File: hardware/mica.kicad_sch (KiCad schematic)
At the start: 29 parts, among them J1 USB_C_Receptacle_USB2.0, J2 Conn_ARM_JTAG_SWD_10, SW1 SW_Push, U1 STM32F072C8Tx, U2 MIC5205-3.3YM5

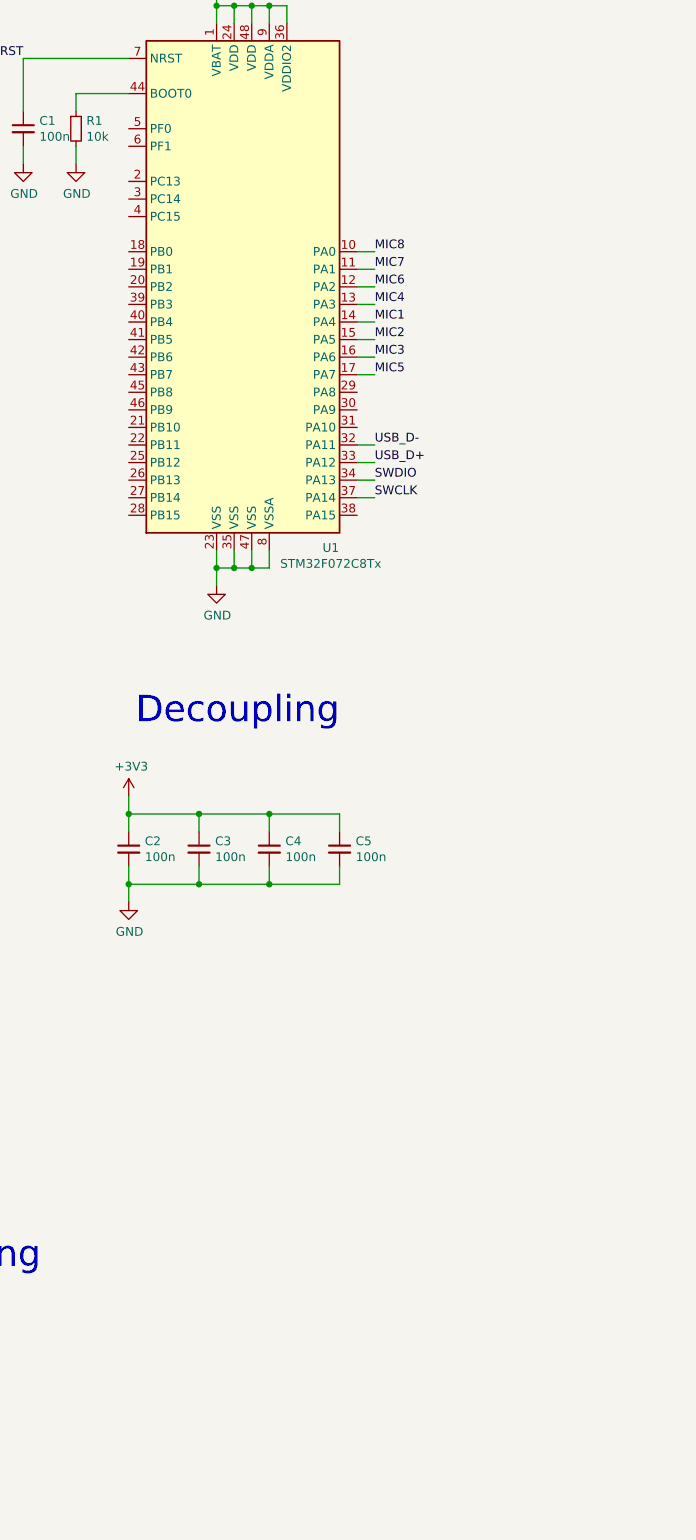
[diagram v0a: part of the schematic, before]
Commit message: Fix all ERC errors
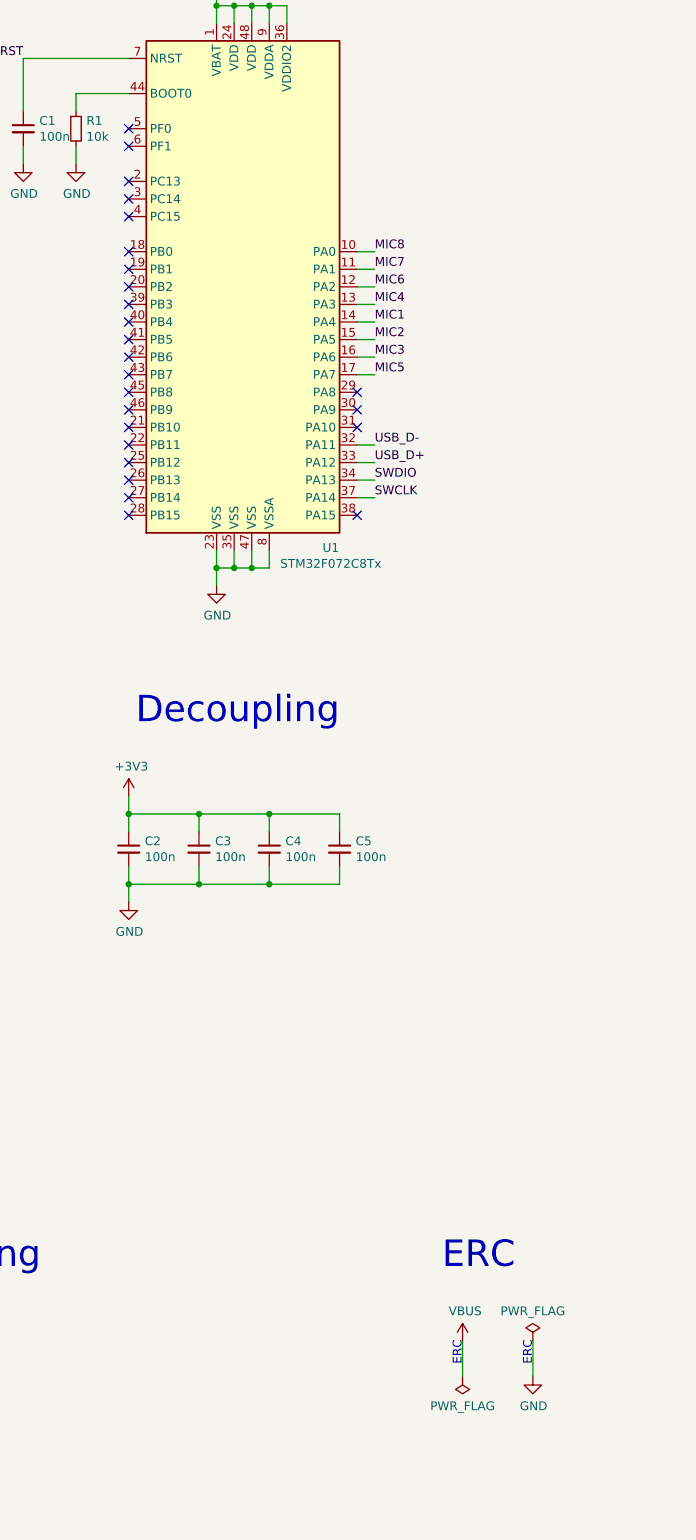
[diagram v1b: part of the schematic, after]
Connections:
- no-connect marks 4 -> 29
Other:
- note added: "ERC"
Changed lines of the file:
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@@
   (junction (at 160.02 86.36) (diameter 0.9144) (color 0 0 0 0))
   (junction (at 218.44 119.38) (diameter 0.9144) (color 0 0 0 0))
+  (no_connect (at 58.42 185.42))
+  (no_connect (at 58.42 187.96))
+  (no_connect (at 58.42 193.04))
+  (no_connect (at 58.42 195.58))
+  (no_connect (at 58.42 198.12))
+  (no_connect (at 58.42 203.2))
+  (no_connect (at 58.42 205.74))
+  (no_connect (at 58.42 208.28))
+  (no_connect (at 58.42 210.82))
+  (no_connect (at 58.42 213.36))
+  (no_connect (at 58.42 215.9))
+  (no_connect (at 58.42 218.44))
+  (no_connect (at 58.42 220.98))
+  (no_connect (at 58.42 223.52))
+  (no_connect (at 58.42 226.06))
+  (no_connect (at 58.42 228.6))
+  (no_connect (at 58.42 231.14))
+  (no_connect (at 58.42 233.68))
+  (no_connect (at 58.42 236.22))
+  (no_connect (at 58.42 238.76))
+  (no_connect (at 58.42 241.3))
   (no_connect (at 76.2 114.3))
   (no_connect (at 76.2 116.84))
+  (no_connect (at 91.44 223.52))
+  (no_connect (at 91.44 226.06))
+  (no_connect (at 91.44 228.6))
+  (no_connect (at 91.44 241.3))
   (no_connect (at 231.14 104.14))
   (no_connect (at 231.14 106.68))
@@
     (stroke (width 0) (type solid) (color 0 0 0 0))
   )
+  (wire (pts (xy 106.68 360.68) (xy 106.68 365.76))
+    (stroke (width 0) (type solid) (color 0 0 0 0))
+  )
+  (wire (pts (xy 116.84 360.68) (xy 116.84 365.76))
+    (stroke (width 0) (type solid) (color 0 0 0 0))
+  )
   (wire (pts (xy 127 83.82) (xy 127 86.36))
     (stroke (width 0) (type solid) (color 0 0 0 0))
@@
     (effects (font (size 3.81 3.81)) (justify right bottom))
   )
+  (text "ERC" (at 106.68 360.68 270)
+    (effects (font (size 1.27 1.27)) (justify right bottom))
+  )
+  (text "ERC" (at 114.3 350.52 180)
+    (effects (font (size 3.81 3.81)) (justify right bottom))
+  )
+  (text "ERC" (at 116.84 360.68 270)
+    (effects (font (size 1.27 1.27)) (justify right bottom))
+  )
   (text "3.3V regulator" (at 165.1 73.66 180)
     (effects (font (size 3.81 3.81)) (justify right bottom))
@@
     (effects (font (size 1.27 1.27)) (justify left bottom))
   )
+  (symbol (lib_id "power:PWR_FLAG") (at 106.68 365.76 180) (unit 1)
+    (in_bom yes) (on_board yes)
+    (property "Reference" "#FLG0101" (id 0) (at 106.68 367.665 0)
+      (effects (font (size 1.27 1.27)) hide)
+    )
+    (property "Value" "PWR_FLAG" (id 1) (at 106.68 370.0844 0))
+    (property "Footprint" "" (id 2) (at 106.68 365.76 0)
+      (effects (font (size 1.27 1.27)) hide)
+    )
+    (property "Datasheet" "~" (id 3) (at 106.68 365.76 0)
+      (effects (font (size 1.27 1.27)) hide)
+    )
+    (pin "1")
+  )
+  (symbol (lib_id "power:PWR_FLAG") (at 116.84 360.68 0) (unit 1)
+    (in_bom yes) (on_board yes)
+    (property "Reference" "#FLG?" (id 0) (at 116.84 358.775 0)
+      (effects (font (size 1.27 1.27)) hide)
+    )
+    (property "Value" "PWR_FLAG" (id 1) (at 116.84 356.3556 0))
+    (property "Footprint" "" (id 2) (at 116.84 360.68 0)
+      (effects (font (size 1.27 1.27)) hide)
+    )
+    (property "Datasheet" "~" (id 3) (at 116.84 360.68 0)
+      (effects (font (size 1.27 1.27)) hide)
+    )
+    (pin "1")
+  )
   (symbol (lib_id "power:+3V3") (at 58.42 281.94 0) (unit 1)
     (in_bom yes) (on_board yes)
@@
     (pin "1")
   )
+  (symbol (lib_id "power:VBUS") (at 106.68 360.68 0) (unit 1)
+    (in_bom yes) (on_board yes)
+    (property "Reference" "#PWR0140" (id 0) (at 106.68 364.49 0)
+      (effects (font (size 1.27 1.27)) hide)
+    )
+    (property "Value" "VBUS" (id 1) (at 107.0483 356.3556 0))
+    (property "Footprint" "" (id 2) (at 106.68 360.68 0)
+      (effects (font (size 1.27 1.27)) hide)
+    )
+    (property "Datasheet" "" (id 3) (at 106.68 360.68 0)
+      (effects (font (size 1.27 1.27)) hide)
+    )
+    (pin "1")
+  )
   (symbol (lib_id "power:VBUS") (at 127 83.82 0) (unit 1)
     (in_bom yes) (on_board yes)
@@
     )
     (property "Datasheet" "" (id 3) (at 99.06 104.14 0)
+      (effects (font (size 1.27 1.27)) hide)
+    )
+    (pin "1")
+  )
+  (symbol (lib_id "power:GND") (at 116.84 365.76 0) (unit 1)
+    (in_bom yes) (on_board yes)
+    (property "Reference" "#PWR?" (id 0) (at 116.84 372.11 0)
+      (effects (font (size 1.27 1.27)) hide)
+    )
+    (property "Value" "GND" (id 1) (at 116.9543 370.0844 0))
+    (property "Footprint" "" (id 2) (at 116.84 365.76 0)
+      (effects (font (size 1.27 1.27)) hide)
+    )
+    (property "Datasheet" "" (id 3) (at 116.84 365.76 0)
       (effects (font (size 1.27 1.27)) hide)
     )
@@
   )
   (symbol_instances
+    (path "/3aa08106-6228-4d8f-b8fc-92081d282ae1"
+      (reference "#FLG0101") (unit 1) (value "PWR_FLAG") (footprint "")
+    )
+    (path "/cb52e577-50e1-4bad-b009-49bdbe72b262"
+      (reference "#FLG?") (unit 1) (value "PWR_FLAG") (footprint "")
+    )
     (path "/ecbc8434-dd2d-4b30-a9cc-c58a56058b10"
       (reference "#PWR01") (unit 1) (value "GND") (footprint "")
@@
       (reference "#PWR019") (unit 1) (value "+3V3") (footprint "")
     )
+    (path "/1e0ff577-e611-44f3-8708-d88e045903c0"
+      (reference "#PWR0140") (unit 1) (value "VBUS") (footprint "")
+    )
+    (path "/2bf07272-5fec-49bc-a787-04a8c4649f10"
+      (reference "#PWR?") (unit 1) (value "GND") (footprint "")
+    )
     (path "/96a8602f-0762-4f84-9239-5b1519e271de"

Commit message: Assign footprints
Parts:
- C1, C2, C3, C4, C5: footprint (none) -> Capacitor_SMD:C_0402_1005Metric; Dielectric - -> X7R; MPN (none) -> 885012205018; Voltage 6.3V -> 10V
- C6, C8: footprint (none) -> Capacitor_SMD:C_0402_1005Metric; Dielectric - -> X7R; MPN (none) -> CL05A225MQ5NNNC; Tolerance 10% -> 20%
- C7: footprint (none) -> Capacitor_SMD:C_0402_1005Metric; Dielectric - -> X7R; MPN (none) -> 885012205059; Voltage 6.3V -> 50V
- D1: footprint (none) -> LED_SMD:LED_0603_1608Metric; MPN (none) -> 150060RS75000
- D2: footprint (none) -> LED_SMD:LED_0603_1608Metric; MPN (none) -> 150060GS75000
- F1: footprint (none) -> Fuse:Fuse_1206_3216Metric; MPN (none) -> PTS120660V005
- J1: MPN (none) -> TYPE-C-31-M-12
- J2: MPN (none) -> FTSH-105-01-L-DV-007-K

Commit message: Place button and leds pins
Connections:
- net BTN_USER: now also U1.26 (PB13)
- net LED_GREEN: now also U1.28 (PB15)
- net LED_RED: now also U1.27 (PB14)
- no-connect marks 29 -> 26

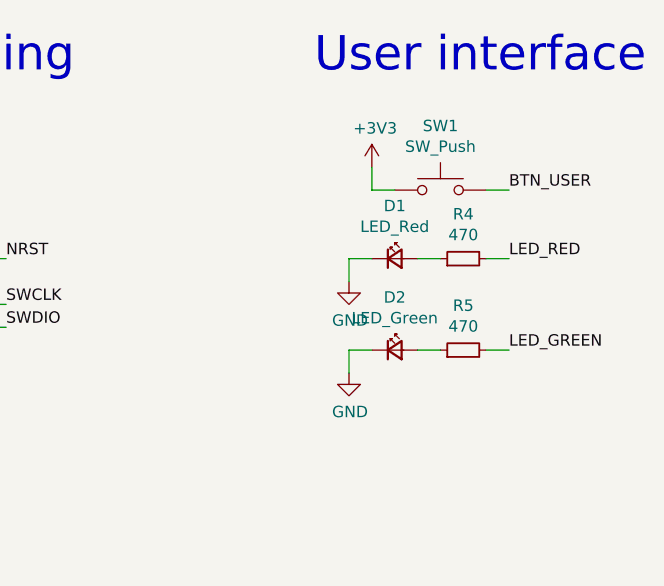
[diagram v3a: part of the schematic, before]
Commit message: Assign all footprints
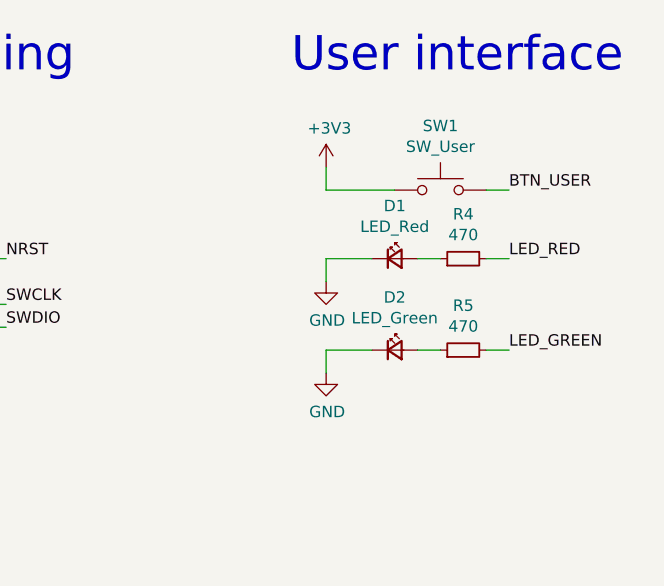
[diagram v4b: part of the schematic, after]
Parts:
- H1, H2, H3, H4, H5, H6, H7, H8: footprint (none) -> MountingHole:MountingHole_3.2mm_M3
- J2: footprint (none) -> User:Samtec_FTSH-105-01-L-DV-K; MPN FTSH-105-01-L-DV-007-K -> FTSH-105-01-L-DV-K
- R1, R2, R3, R4, R5: footprint (none) -> Resistor_SMD:R_0402_1005Metric
- SW1: value SW_Push -> SW_User; footprint (none) -> Button_Switch_THT:SW_PUSH_6mm

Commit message: Remove 4 of the 8 mounting holes
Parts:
- removed H5, H6, H7, H8: MountingHole, MountingHole:MountingHole_3.2mm_M3, symbol Mechanical:MountingHole
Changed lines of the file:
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@@
-    )
-  )
-  (symbol (lib_id "Mechanical:MountingHole") (at 22.86 381 0) (unit 1)
-    (in_bom yes) (on_board yes)
-    (property "Reference" "H5" (id 0) (at 25.4001 379.8506 0)
-      (effects (font (size 1.27 1.27)) (justify left))
-    )
-    (property "Value" "MountingHole" (id 1) (at 25.4001 382.1493 0)
-      (effects (font (size 1.27 1.27)) (justify left))
-    )
-    (property "Footprint" "MountingHole:MountingHole_3.2mm_M3" (id 2) (at 22.86 381 0)
-      (effects (font (size 1.27 1.27)) hide)
-    )
-    (property "Datasheet" "~" (id 3) (at 22.86 381 0)
-      (effects (font (size 1.27 1.27)) hide)
-    )
-  )
-  (symbol (lib_id "Mechanical:MountingHole") (at 22.86 386.08 0) (unit 1)
-    (in_bom yes) (on_board yes)
-    (property "Reference" "H6" (id 0) (at 25.4001 384.9306 0)
-      (effects (font (size 1.27 1.27)) (justify left))
-    )
-    (property "Value" "MountingHole" (id 1) (at 25.4001 387.2293 0)
-      (effects (font (size 1.27 1.27)) (justify left))
-    )
-    (property "Footprint" "MountingHole:MountingHole_3.2mm_M3" (id 2) (at 22.86 386.08 0)
-      (effects (font (size 1.27 1.27)) hide)
-    )
-    (property "Datasheet" "~" (id 3) (at 22.86 386.08 0)
-      (effects (font (size 1.27 1.27)) hide)
-    )
-  )
-  (symbol (lib_id "Mechanical:MountingHole") (at 22.86 391.16 0) (unit 1)
-    (in_bom yes) (on_board yes)
-    (property "Reference" "H7" (id 0) (at 25.4001 390.0106 0)
-      (effects (font (size 1.27 1.27)) (justify left))
-    )
-    (property "Value" "MountingHole" (id 1) (at 25.4001 392.3093 0)
-      (effects (font (size 1.27 1.27)) (justify left))
-    )
-    (property "Footprint" "MountingHole:MountingHole_3.2mm_M3" (id 2) (at 22.86 391.16 0)
-      (effects (font (size 1.27 1.27)) hide)
-    )
-    (property "Datasheet" "~" (id 3) (at 22.86 391.16 0)
-      (effects (font (size 1.27 1.27)) hide)
-    )
-  )
-  (symbol (lib_id "Mechanical:MountingHole") (at 22.86 396.24 0) (unit 1)
-    (in_bom yes) (on_board yes)
-    (property "Reference" "H8" (id 0) (at 25.4001 395.0906 0)
-      (effects (font (size 1.27 1.27)) (justify left))
-    )
-    (property "Value" "MountingHole" (id 1) (at 25.4001 397.3893 0)
-      (effects (font (size 1.27 1.27)) (justify left))
-    )
-    (property "Footprint" "MountingHole:MountingHole_3.2mm_M3" (id 2) (at 22.86 396.24 0)
-      (effects (font (size 1.27 1.27)) hide)
-    )
-    (property "Datasheet" "~" (id 3) (at 22.86 396.24 0)
-      (effects (font (size 1.27 1.27)) hide)
     )
   )
@@
       (reference "H4") (unit 1) (value "MountingHole") (footprint "MountingHole:MountingHole_3.2mm_M3")
     )
-    (path "/319baa0e-3118-4d58-98db-abbb454a61e6"
-      (reference "H5") (unit 1) (value "MountingHole") (footprint "MountingHole:MountingHole_3.2mm_M3")
-    )
-    (path "/f24bdbeb-cd21-4868-8b07-ee9ec1d1eb89"
-      (reference "H6") (unit 1) (value "MountingHole") (footprint "MountingHole:MountingHole_3.2mm_M3")
-    )
-    (path "/c1f9fd7b-3194-4c18-b9b0-d98fdc9f7b08"
-      (reference "H7") (unit 1) (value "MountingHole") (footprint "MountingHole:MountingHole_3.2mm_M3")
-    )
-    (path "/7a5c6f56-f8b8-4653-be2a-64d41c8a2f27"
-      (reference "H8") (unit 1) (value "MountingHole") (footprint "MountingHole:MountingHole_3.2mm_M3")
-    )
     (path "/2acd2377-0622-41af-a5c8-24d6ac3d4787"
